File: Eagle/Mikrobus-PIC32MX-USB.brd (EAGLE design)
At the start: 28.2 x 58.7 mm, 33 parts, among them U1 PIC32MX250F128B-I_SP, X1 8Mhz

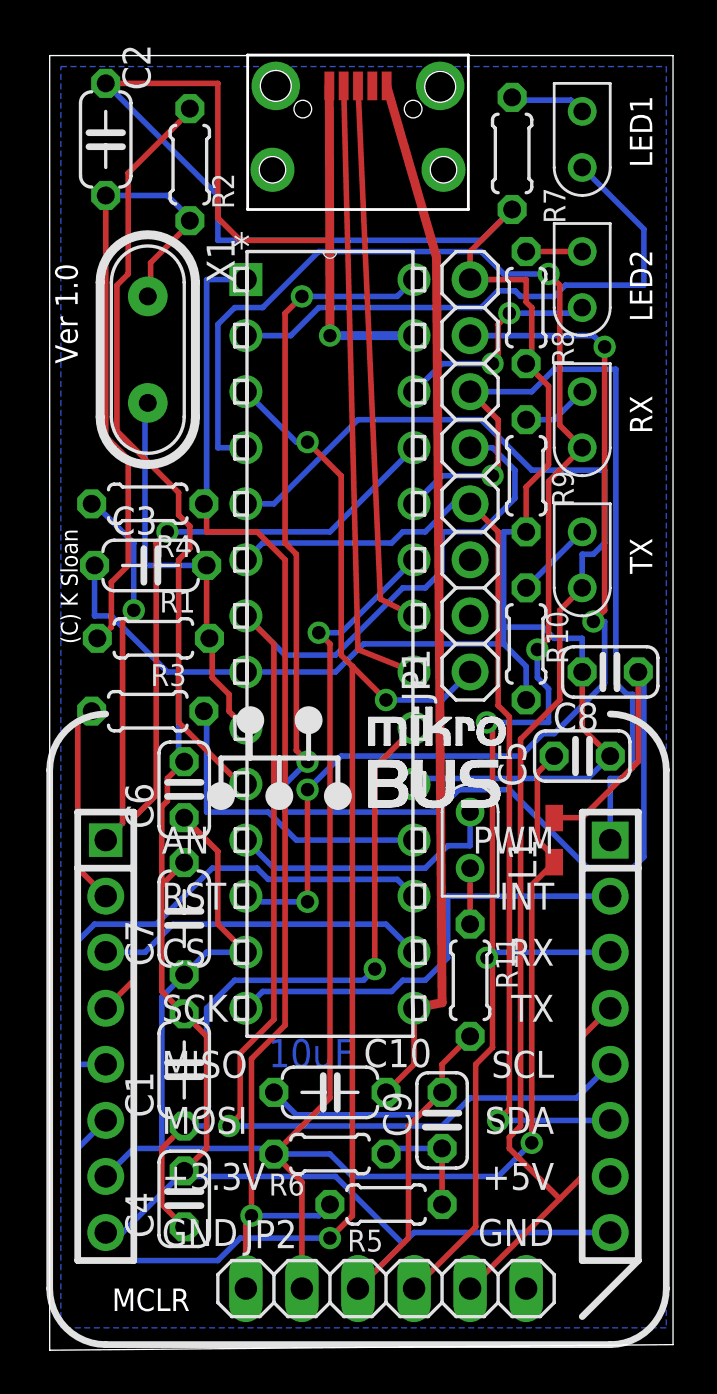
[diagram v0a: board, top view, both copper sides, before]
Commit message: Correction USB connector orientation
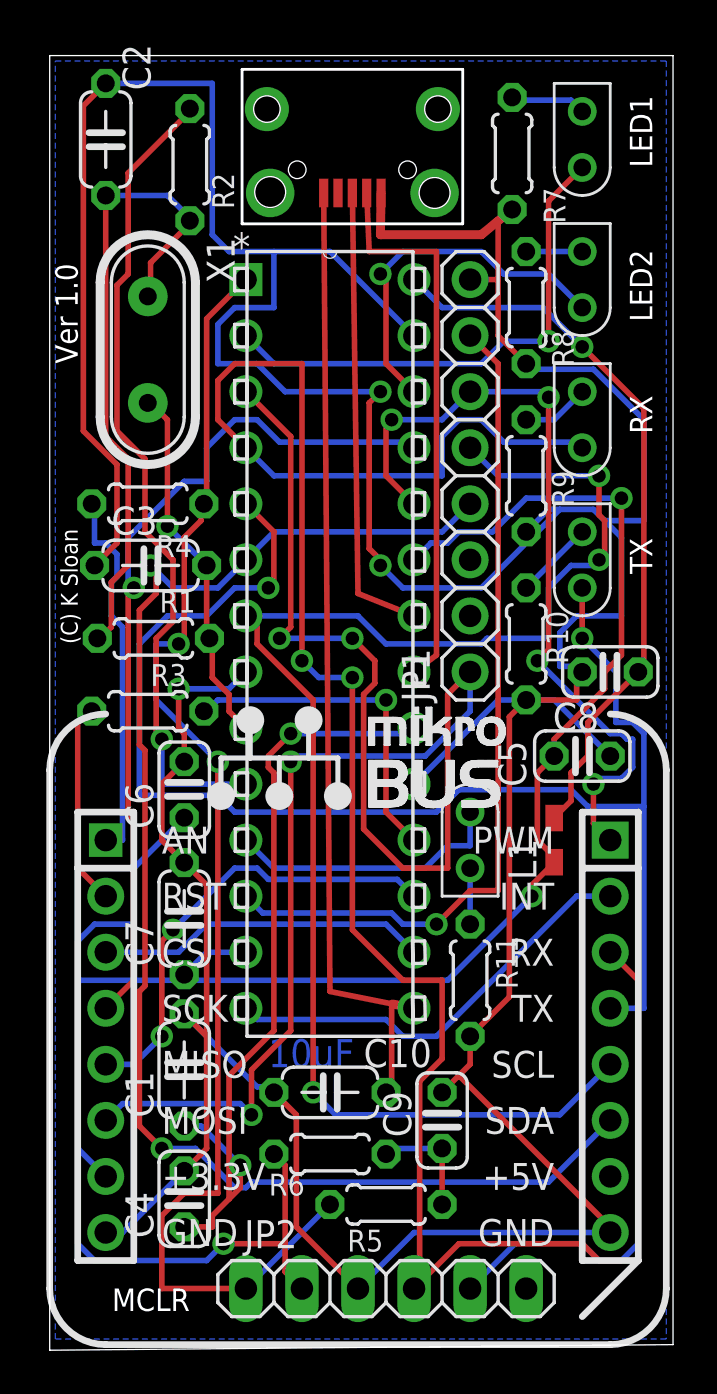
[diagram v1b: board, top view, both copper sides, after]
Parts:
- moved USB1 6.36 mm to (13.7, 57.8), turned to 180 degrees
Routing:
- net AVDD: track 65.9 -> 33.1 mm, vias 2 -> 1
- net GND: track 201.2 -> 229.4 mm, vias 1 -> 3
- net SDA: track 45.2 -> 66.3 mm, vias 1 -> 2
- net RX/PGED: track 81.7 -> 98.5 mm, vias 4 -> 2
- net TX/PGEC: track 70.2 -> 84.0 mm, vias 0 -> 2
- net RA4: track 45.7 -> 38.3 mm, vias 4 -> 1
- net MOSI: track 66.3 -> 73.4 mm, vias 3 -> 4
- net LED2: track 10.1 -> 16.6 mm, vias 2 -> 1
- net MCLR: track 55.1 -> 60.4 mm, vias 1 -> 2
- net VCAP: track 31.8 -> 36.0 mm, vias 1 -> 2
- net D-: track 25.0 -> 20.9 mm
- net SCL: track 63.5 -> 67.5 mm, vias 1 -> 3
- net SCK: track 35.5 -> 38.9 mm
- net VBUS: track 47.5 -> 44.2 mm
- net MISO: track 24.0 -> 20.7 mm, vias 0 -> 2
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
